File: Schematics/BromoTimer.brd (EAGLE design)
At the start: 101.6 x 80 mm, 29 parts, among them IC1 PIC16F687, IC2 7805TV, K1 G2R2A, K2 G2R2A, Q1 BC548B, Q2 BC548B, Q3 BC548B, X1 AC_IN, X4 22-23-2041, X5 AC_OUT

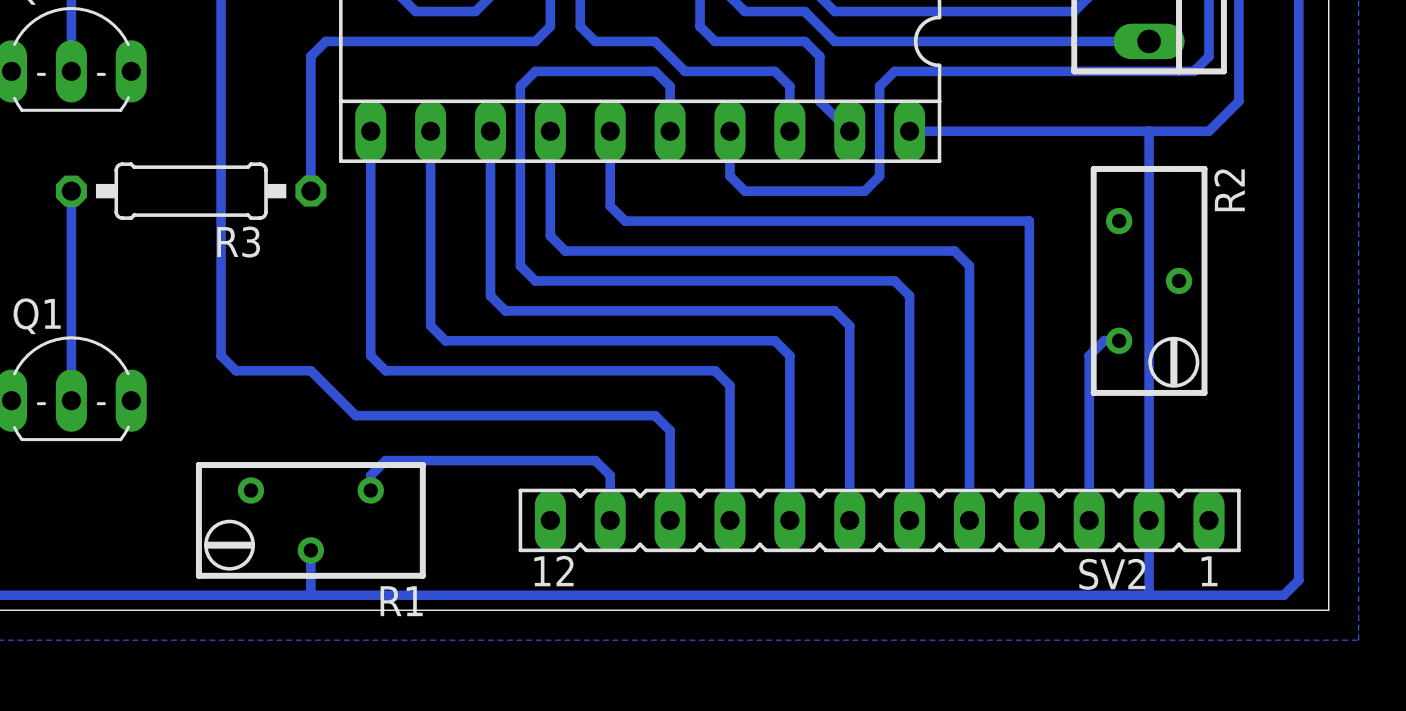
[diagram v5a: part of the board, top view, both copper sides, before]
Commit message: Correct trimmer footprints
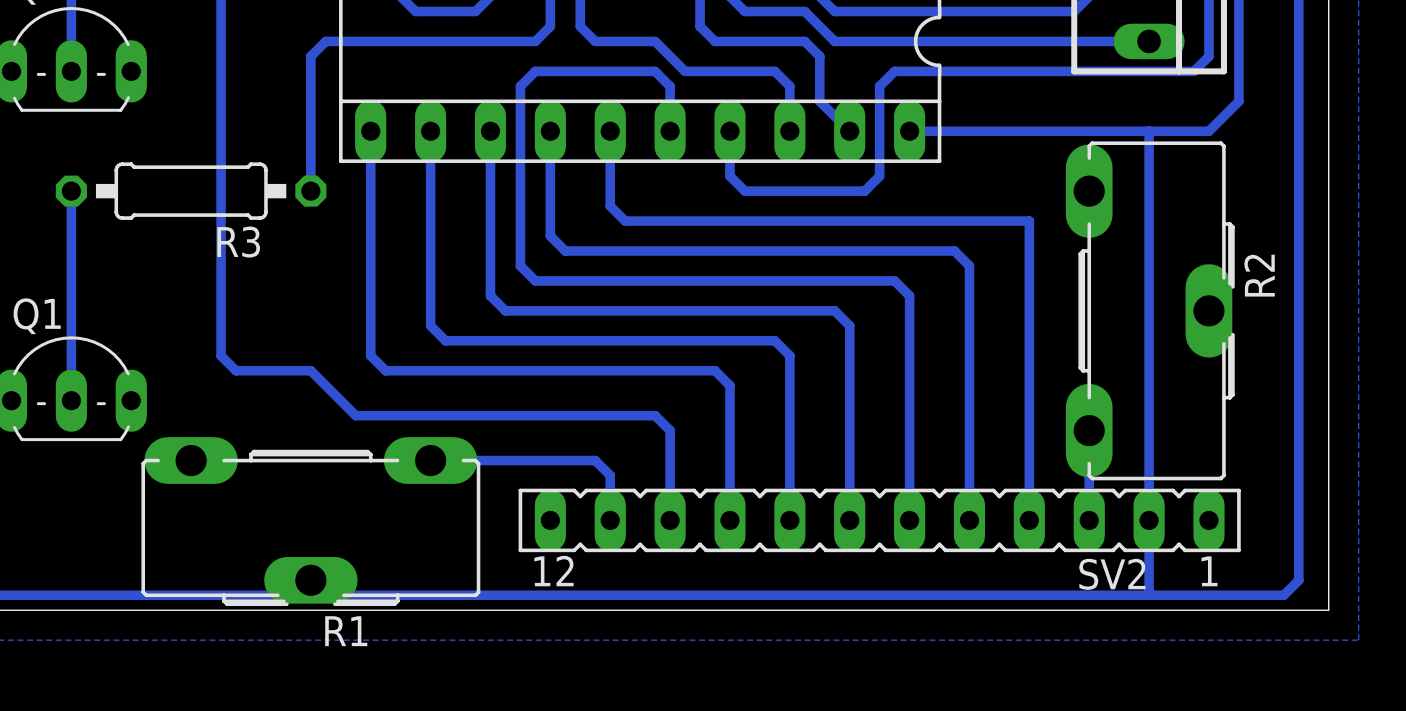
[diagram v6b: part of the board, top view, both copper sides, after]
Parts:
- R1, R2: device rcl:RTRIMT93YB -> pot:CA14H
- moved R2 2.84 mm to (91.4, 12.7), turned to 270 degrees
- moved R1 2.54 mm to (58.4, 6.35), turned to 180 degrees
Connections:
- net +5V: now also R1.S; no longer R1.2
- net GND: now also R2.S; no longer R2.2
- net N$1: now also R1.A; no longer R1.1
- net N$3: now also R2.E; no longer R2.3
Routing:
- net N$3: track 8.52 -> 3.81 mm
- net N$1: track 13.2 -> 9.79 mm
- net +5V: track 287.8 -> 286.6 mm
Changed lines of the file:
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@@
 <layer number="18" name="Vias" color="2" fill="1" visible="yes" active="yes"/>
 <layer number="19" name="Unrouted" color="6" fill="1" visible="yes" active="yes"/>
-<layer number="20" name="Dimension" color="15" fill="1" visible="no" active="yes"/>
-<layer number="21" name="tPlace" color="7" fill="1" visible="no" active="yes"/>
-<layer number="22" name="bPlace" color="7" fill="1" visible="no" active="yes"/>
-<layer number="23" name="tOrigins" color="15" fill="1" visible="no" active="yes"/>
-<layer number="24" name="bOrigins" color="15" fill="1" visible="no" active="yes"/>
-<layer number="25" name="tNames" color="7" fill="1" visible="no" active="yes"/>
-<layer number="26" name="bNames" color="7" fill="1" visible="no" active="yes"/>
-<layer number="27" name="tValues" color="7" fill="1" visible="no" active="yes"/>
-<layer number="28" name="bValues" color="7" fill="1" visible="no" active="yes"/>
+<layer number="20" name="Dimension" color="15" fill="1" visible="yes" active="yes"/>
+<layer number="21" name="tPlace" color="7" fill="1" visible="yes" active="yes"/>
+<layer number="22" name="bPlace" color="7" fill="1" visible="yes" active="yes"/>
+<layer number="23" name="tOrigins" color="15" fill="1" visible="yes" active="yes"/>
+<layer number="24" name="bOrigins" color="15" fill="1" visible="yes" active="yes"/>
+<layer number="25" name="tNames" color="7" fill="1" visible="yes" active="yes"/>
+<layer number="26" name="bNames" color="7" fill="1" visible="yes" active="yes"/>
+<layer number="27" name="tValues" color="7" fill="1" visible="yes" active="yes"/>
+<layer number="28" name="bValues" color="7" fill="1" visible="yes" active="yes"/>
 <layer number="29" name="tStop" color="7" fill="3" visible="no" active="yes"/>
 <layer number="30" name="bStop" color="7" fill="6" visible="no" active="yes"/>
@@
 <layer number="37" name="tTest" color="7" fill="1" visible="no" active="yes"/>
 <layer number="38" name="bTest" color="7" fill="1" visible="no" active="yes"/>
-<layer number="39" name="tKeepout" color="4" fill="11" visible="no" active="yes"/>
-<layer number="40" name="bKeepout" color="1" fill="11" visible="no" active="yes"/>
-<layer number="41" name="tRestrict" color="4" fill="10" visible="no" active="yes"/>
-<layer number="42" name="bRestrict" color="1" fill="10" visible="no" active="yes"/>
-<layer number="43" name="vRestrict" color="2" fill="10" visible="no" active="yes"/>
+<layer number="39" name="tKeepout" color="4" fill="11" visible="yes" active="yes"/>
+<layer number="40" name="bKeepout" color="1" fill="11" visible="yes" active="yes"/>
+<layer number="41" name="tRestrict" color="4" fill="10" visible="yes" active="yes"/>
+<layer number="42" name="bRestrict" color="1" fill="10" visible="yes" active="yes"/>
+<layer number="43" name="vRestrict" color="2" fill="10" visible="yes" active="yes"/>
 <layer number="44" name="Drills" color="7" fill="1" visible="no" active="yes"/>
 <layer number="45" name="Holes" color="7" fill="1" visible="no" active="yes"/>
 <layer number="46" name="Milling" color="3" fill="1" visible="no" active="yes"/>
 <layer number="47" name="Measures" color="7" fill="1" visible="no" active="yes"/>
-<layer number="48" name="Document" color="7" fill="1" visible="no" active="yes"/>
-<layer number="49" name="Reference" color="7" fill="1" visible="no" active="yes"/>
+<layer number="48" name="Document" color="7" fill="1" visible="yes" active="yes"/>
+<layer number="49" name="Reference" color="7" fill="1" visible="yes" active="yes"/>
 <layer number="50" name="dxf" color="7" fill="1" visible="no" active="no"/>
-<layer number="51" name="tDocu" color="7" fill="1" visible="no" active="yes"/>
-<layer number="52" name="bDocu" color="7" fill="1" visible="no" active="yes"/>
+<layer number="51" name="tDocu" color="7" fill="1" visible="yes" active="yes"/>
+<layer number="52" name="bDocu" color="7" fill="1" visible="yes" active="yes"/>
 <layer number="53" name="tGND_GNDA" color="7" fill="9" visible="no" active="no"/>
 <layer number="54" name="bGND_GNDA" color="1" fill="9" visible="no" active="no"/>
@@
 <element name="C1" library="rcl" package="E5-13" value="1m" x="71.12" y="72.39" rot="R270"/>
 <element name="C2" library="rcl" package="C025-024X044" value="100n" x="88.9" y="63.5" rot="R180"/>
-<element name="R1" library="rcl" package="RTRIMT93YB" value="100k" x="58.42" y="3.81" rot="R90"/>
-<element name="R2" library="rcl" package="RTRIMT93YB" value="100k" x="93.98" y="13.97" rot="R180"/>
+<element name="R1" library="pot" package="CA14H" value="100k" x="58.42" y="6.35" rot="R180"/>
+<element name="R2" library="pot" package="CA14H" value="100k" x="91.44" y="12.7" rot="R270"/>
 <element name="Q1" library="transistor-npn" package="TO92-EBC" value="BC548B" x="48.26" y="10.16"/>
 <element name="Q2" library="transistor-npn" package="TO92-EBC" value="BC548B" x="48.26" y="24.13"/>
@@
 <wire x1="96.52" y1="20.32" x2="93.98" y2="20.32" width="0.4064" layer="16"/>
 <wire x1="34.29" y1="1.27" x2="34.29" y2="16.51" width="0.4064" layer="16"/>
-<contactref element="R1" pad="2"/>
-<wire x1="58.42" y1="2.54" x2="58.42" y2="0.635" width="0.4064" layer="16"/>
+<contactref element="R1" pad="S"/>
+<wire x1="58.42" y1="1.27" x2="58.42" y2="0.635" width="0.4064" layer="16"/>
 </signal>
 <signal name="GND">
@@
 <contactref element="IC1" pad="1"/>
 <contactref element="SV2" pad="1"/>
-<contactref element="R2" pad="2"/>
 <contactref element="SV2" pad="12"/>
 <contactref element="Q1" pad="E"/>
@@
 </polygon>
 <contactref element="X4" pad="1"/>
+<contactref element="R2" pad="S"/>
 </signal>
 <signal name="RS">
@@
 <wire x1="54.61" y1="27.305" x2="55.245" y2="27.94" width="0.4064" layer="16"/>
 <wire x1="55.245" y1="27.94" x2="60.96" y2="27.94" width="0.4064" layer="16"/>
-</signal>
-<signal name="N$1">
-<contactref element="SV2" pad="11"/>
-<contactref element="R1" pad="1"/>
-<wire x1="71.12" y1="3.81" x2="71.12" y2="5.715" width="0.4064" layer="16"/>
-<wire x1="71.12" y1="5.715" x2="70.485" y2="6.35" width="0.4064" layer="16"/>
-<wire x1="70.485" y1="6.35" x2="61.595" y2="6.35" width="0.4064" layer="16"/>
-<wire x1="61.595" y1="6.35" x2="60.96" y2="5.715" width="0.4064" layer="16"/>
-<wire x1="60.96" y1="5.715" x2="60.96" y2="5.08" width="0.4064" layer="16"/>
-</signal>
-<signal name="N$3">
-<contactref element="SV2" pad="3"/>
-<contactref element="R2" pad="3"/>
-<wire x1="91.44" y1="3.81" x2="91.44" y2="10.795" width="0.4064" layer="16"/>
-<wire x1="91.44" y1="10.795" x2="92.075" y2="11.43" width="0.4064" layer="16"/>
-<wire x1="92.075" y1="11.43" x2="92.71" y2="11.43" width="0.4064" layer="16"/>
 </signal>
 <signal name="L1">
@@
 <wire x1="88.265" y1="29.21" x2="93.98" y2="29.21" width="0.4064" layer="16"/>
 </signal>
+<signal name="N$3">
+<contactref element="SV2" pad="3"/>
+<contactref element="R2" pad="E"/>
+<wire x1="91.44" y1="3.81" x2="91.44" y2="7.62" width="0.4064" layer="16"/>
+</signal>
+<signal name="N$1">
+<contactref element="SV2" pad="11"/>
+<contactref element="R1" pad="A"/>
+<wire x1="63.5" y1="6.35" x2="70.485" y2="6.35" width="0.4064" layer="16"/>
+<wire x1="70.485" y1="6.35" x2="71.12" y2="5.715" width="0.4064" layer="16"/>
+<wire x1="71.12" y1="5.715" x2="71.12" y2="3.81" width="0.4064" layer="16"/>
+</signal>
 </signals>

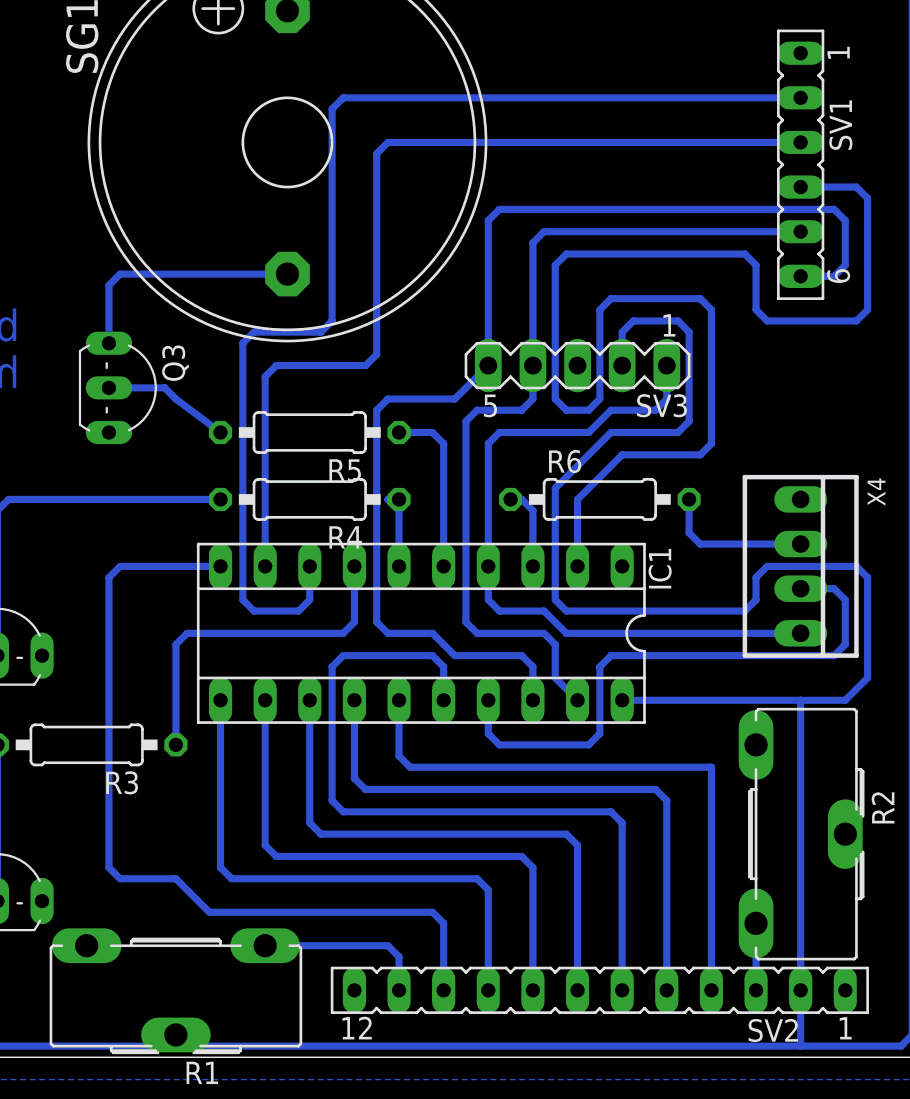
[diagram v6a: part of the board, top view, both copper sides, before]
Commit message: Increase default keepout
Default keepout increased to 25mil. Also, inverted function of RC6 and RC7.
Change is also made in code to reflect this.
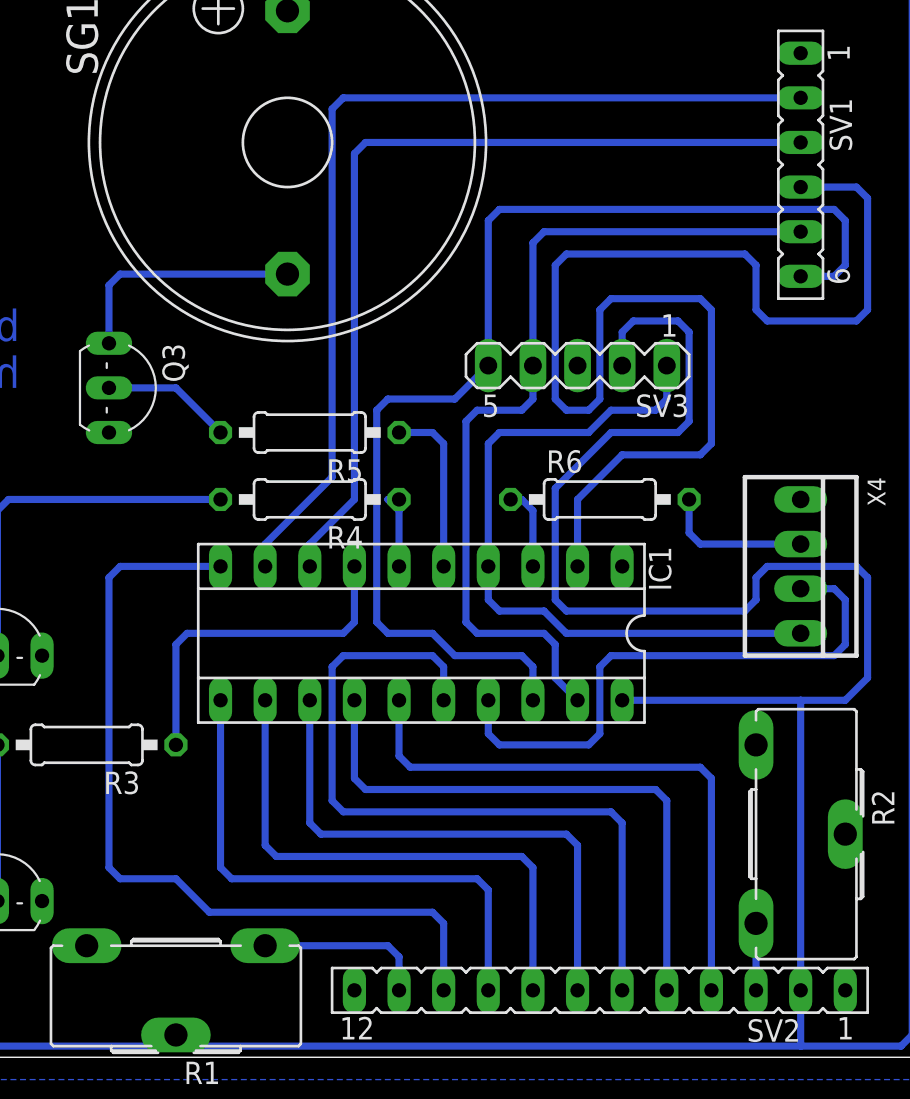
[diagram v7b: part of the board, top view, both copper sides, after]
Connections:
- net L1: now also IC1.9; no longer IC1.8
- net L2: now also IC1.8; no longer IC1.9
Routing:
- net L1: track 65.5 -> 54.5 mm
- net L2: track 53.5 -> 50.2 mm
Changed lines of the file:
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@@
 <classes>
 <class number="0" name="default" width="0.4064" drill="0">
-<clearance class="0" value="0.4064"/>
+<clearance class="0" value="0.635"/>
 </class>
 <class number="1" name="HV" width="1.27" drill="0">
@@
 <contactref element="SV2" pad="4"/>
 <contactref element="IC1" pad="15"/>
-<wire x1="88.9" y1="3.81" x2="88.9" y2="16.51" width="0.4064" layer="16"/>
-<wire x1="88.9" y1="16.51" x2="71.755" y2="16.51" width="0.4064" layer="16"/>
+<wire x1="88.9" y1="3.81" x2="88.9" y2="15.875" width="0.4064" layer="16"/>
+<wire x1="88.9" y1="15.875" x2="88.265" y2="16.51" width="0.4064" layer="16"/>
+<wire x1="88.265" y1="16.51" x2="71.755" y2="16.51" width="0.4064" layer="16"/>
 <wire x1="71.755" y1="16.51" x2="71.12" y2="17.145" width="0.4064" layer="16"/>
 <wire x1="71.12" y1="17.145" x2="71.12" y2="20.32" width="0.4064" layer="16"/>
@@
 <signal name="L1">
 <contactref element="SV1" pad="2"/>
-<contactref element="IC1" pad="8"/>
 <wire x1="93.98" y1="54.61" x2="67.945" y2="54.61" width="0.4064" layer="16"/>
 <wire x1="67.945" y1="54.61" x2="67.31" y2="53.975" width="0.4064" layer="16"/>
-<wire x1="67.31" y1="53.975" x2="67.31" y2="41.91" width="0.4064" layer="16"/>
-<wire x1="67.31" y1="41.91" x2="66.675" y2="41.275" width="0.4064" layer="16"/>
-<wire x1="66.675" y1="41.275" x2="62.865" y2="41.275" width="0.4064" layer="16"/>
-<wire x1="62.865" y1="41.275" x2="62.23" y2="40.64" width="0.4064" layer="16"/>
-<wire x1="62.23" y1="40.64" x2="62.23" y2="26.035" width="0.4064" layer="16"/>
-<wire x1="62.23" y1="26.035" x2="62.865" y2="25.4" width="0.4064" layer="16"/>
-<wire x1="62.865" y1="25.4" x2="65.405" y2="25.4" width="0.4064" layer="16"/>
-<wire x1="65.405" y1="25.4" x2="66.04" y2="26.035" width="0.4064" layer="16"/>
-<wire x1="66.04" y1="26.035" x2="66.04" y2="27.94" width="0.4064" layer="16"/>
+<contactref element="IC1" pad="9"/>
+<wire x1="63.5" y1="27.94" x2="63.5" y2="29.21" width="0.4064" layer="16"/>
+<wire x1="67.31" y1="33.02" x2="63.5" y2="29.21" width="0.4064" layer="16"/>
+<wire x1="67.31" y1="33.02" x2="67.31" y2="53.975" width="0.4064" layer="16"/>
 </signal>
 <signal name="L2">
 <contactref element="SV1" pad="3"/>
-<contactref element="IC1" pad="9"/>
-<wire x1="93.98" y1="52.07" x2="70.485" y2="52.07" width="0.4064" layer="16"/>
-<wire x1="70.485" y1="52.07" x2="69.85" y2="51.435" width="0.4064" layer="16"/>
-<wire x1="69.85" y1="51.435" x2="69.85" y2="40.005" width="0.4064" layer="16"/>
-<wire x1="69.85" y1="40.005" x2="69.215" y2="39.37" width="0.4064" layer="16"/>
-<wire x1="69.215" y1="39.37" x2="64.135" y2="39.37" width="0.4064" layer="16"/>
-<wire x1="64.135" y1="39.37" x2="63.5" y2="38.735" width="0.4064" layer="16"/>
-<wire x1="63.5" y1="38.735" x2="63.5" y2="27.94" width="0.4064" layer="16"/>
+<wire x1="93.98" y1="52.07" x2="69.215" y2="52.07" width="0.4064" layer="16"/>
+<wire x1="69.215" y1="52.07" x2="68.58" y2="51.435" width="0.4064" layer="16"/>
+<wire x1="68.58" y1="51.435" x2="68.58" y2="31.75" width="0.4064" layer="16"/>
+<contactref element="IC1" pad="8"/>
+<wire x1="68.58" y1="31.75" x2="66.04" y2="29.21" width="0.4064" layer="16"/>
+<wire x1="66.04" y1="29.21" x2="66.04" y2="27.94" width="0.4064" layer="16"/>
 </signal>
 <signal name="SW">
@@
 <contactref element="Q3" pad="B"/>
 <contactref element="R5" pad="2"/>
-<wire x1="54.61" y1="38.1" x2="57.785" y2="38.1" width="0.4064" layer="16"/>
-<wire x1="57.785" y1="38.1" x2="58.42" y2="37.465" width="0.4064" layer="16"/>
-<wire x1="58.42" y1="37.465" x2="60.96" y2="35.56" width="0.4064" layer="16"/>
+<wire x1="54.61" y1="38.1" x2="58.42" y2="38.1" width="0.4064" layer="16"/>
+<wire x1="58.42" y1="38.1" x2="60.96" y2="35.56" width="0.4064" layer="16"/>
 </signal>
 <signal name="N$19">
